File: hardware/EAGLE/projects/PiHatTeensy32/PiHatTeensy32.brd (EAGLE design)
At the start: 100 x 80 mm, 16 parts, among them T4 BM08B-SRSS-TB, U1 TSR_1-2450, X1 RASPI_BOARD_B+_H

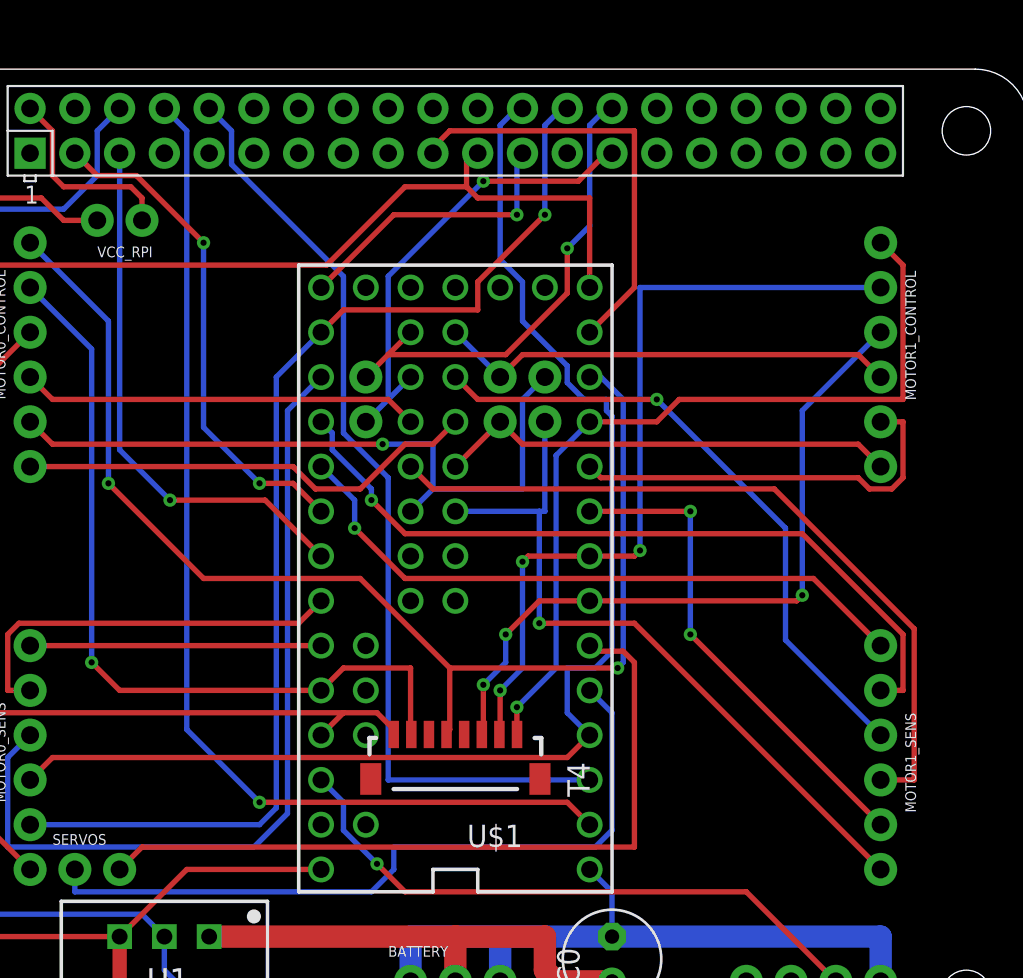
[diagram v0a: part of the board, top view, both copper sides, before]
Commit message: cancelled UART, made some cosmetic changes, ready for production
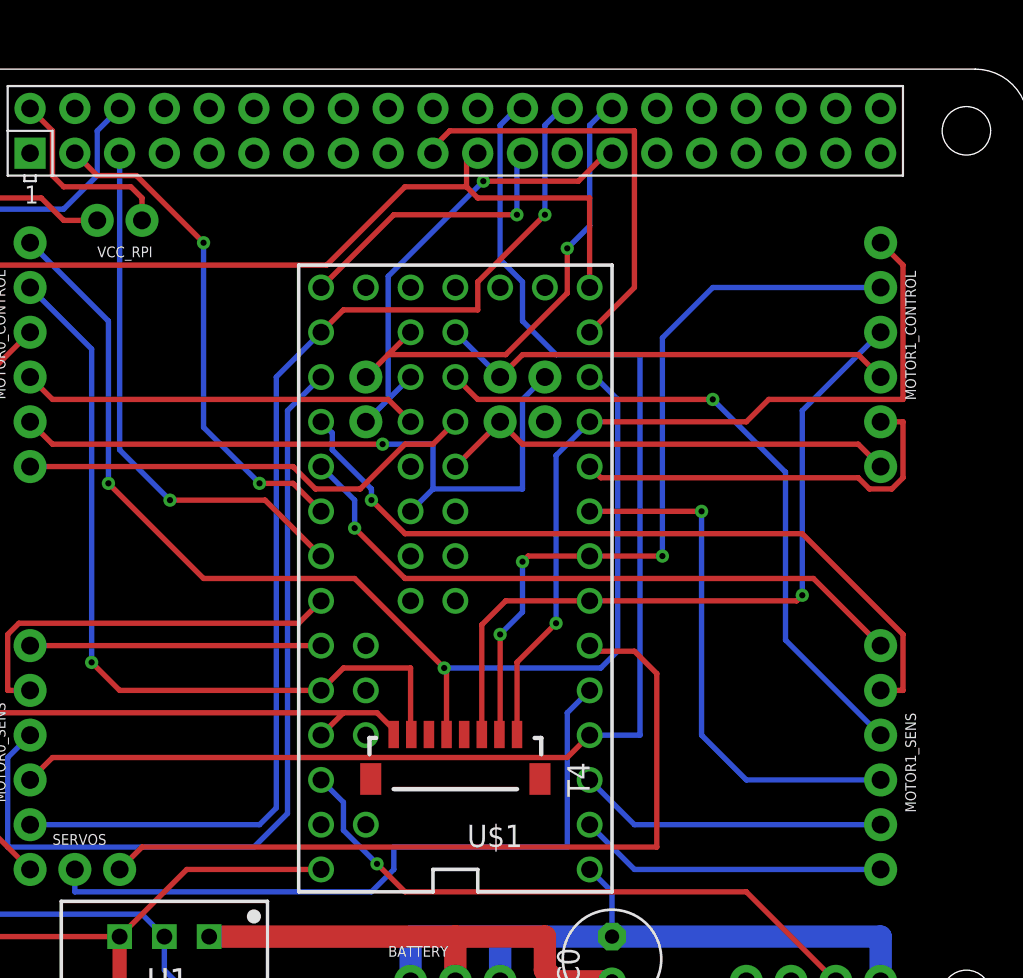
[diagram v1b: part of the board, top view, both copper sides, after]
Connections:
- net HALL_U1: now also U$1.0; no longer T4-32-33.1, U$1.24
- net HALL_V1: now also U$1.1; no longer U$1.7
- net HALL_W1: now also U$1.7; no longer U$1.32
- net PI_RX: no longer U$1.1
- net PI_TX: no longer U$1.0
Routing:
- net PI_TX: track 60.9 -> 0.00 mm, vias 1 -> 0
- net PI_RX: track 53.7 -> 0.00 mm
- net HALL_U1: track 41.7 -> 17.6 mm, vias 1 -> 0
- net HALL_W1: track 42.9 -> 30.3 mm, vias 0 -> 1
- net HALL_V1: track 28.0 -> 17.6 mm, vias 2 -> 0
- net HALL_W0_&_SPI_CS0: track 75.0 -> 78.0 mm
- net SERVO_1: track 43.2 -> 45.4 mm
- net SERVO_0: track 42.4 -> 40.4 mm
- net IS_U1: track 36.3 -> 38.1 mm
- net IN_V1: track 45.8 -> 44.4 mm
- net IN_U1: track 40.7 -> 41.9 mm, vias 3 -> 1
- net IN_W0: track 70.4 -> 69.4 mm

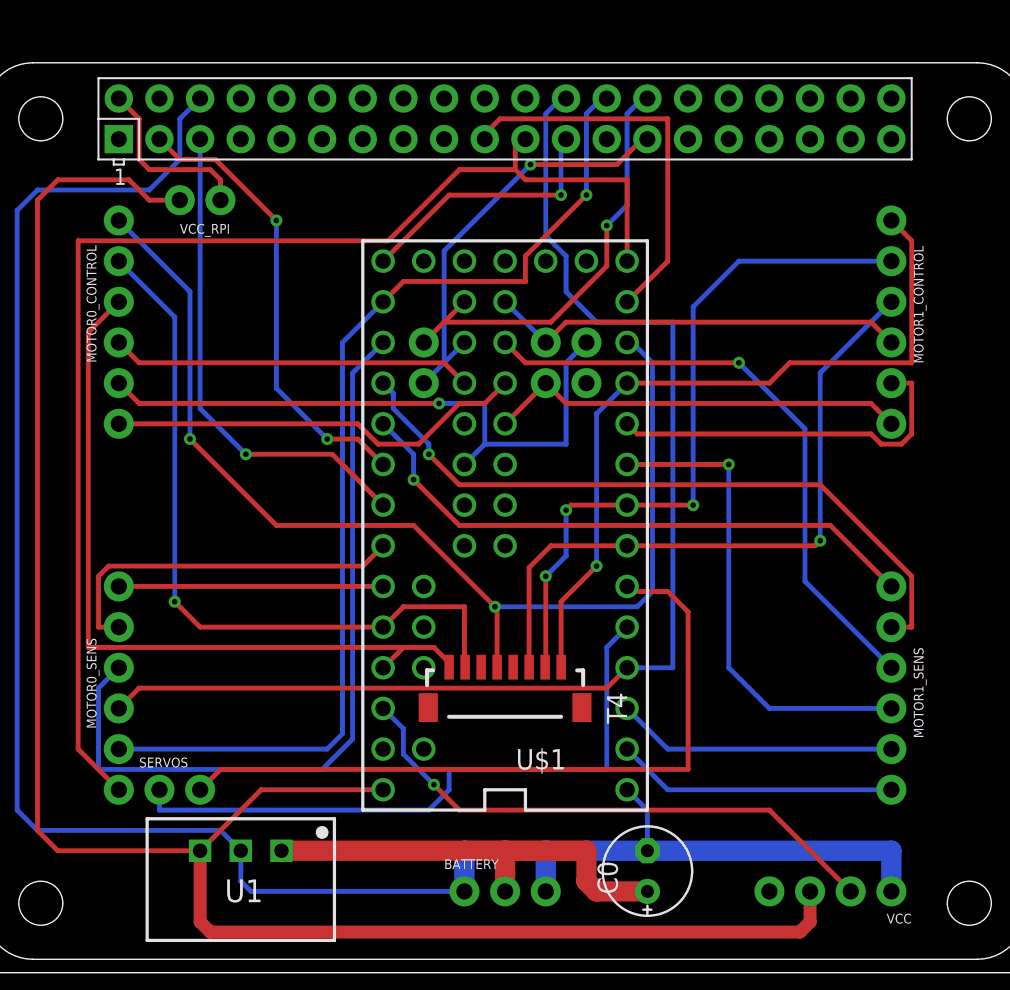
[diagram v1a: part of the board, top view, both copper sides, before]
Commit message: uart tx tx added back again, more coesmetic changes
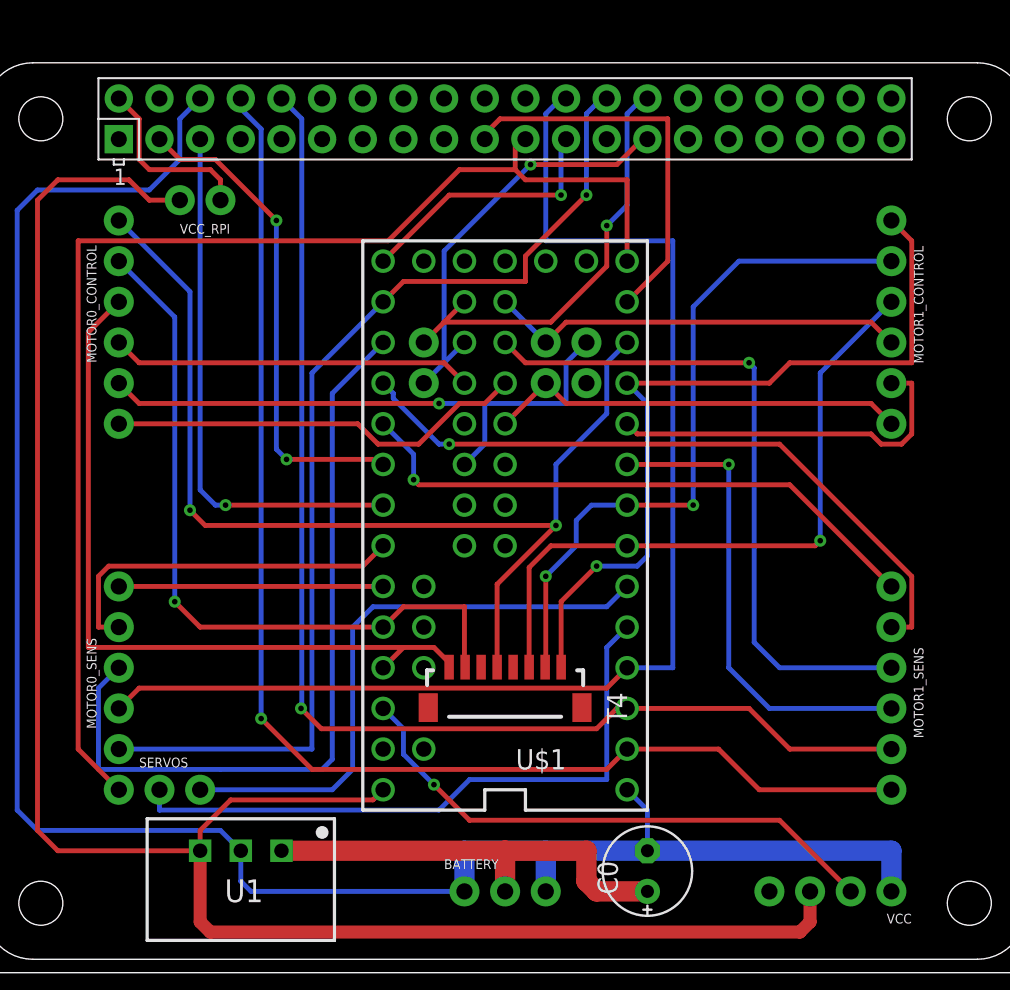
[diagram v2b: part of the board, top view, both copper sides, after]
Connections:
- removed net HALL_U1: MOTOR1_SENS.1, U$1.0
- removed net HALL_V1: MOTOR1_SENS.2, U$1.1
- removed net PI_RX: X1.10
- removed net PI_TX: X1.8
- new net HALL_U1_&_PI_TX: MOTOR1_SENS.1, U$1.0, X1.8
- new net HALL_V1_&PI_RX: MOTOR1_SENS.2, U$1.1, X1.10
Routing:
- net HALL_U1_&_PI_TX: track 0.00 -> 81.5 mm, vias 0 -> 1
- net HALL_V1_&PI_RX: track 0.00 -> 77.7 mm, vias 0 -> 1
- net HALL_V1: track 17.6 -> 0.00 mm
- net HALL_U1: track 17.6 -> 0.00 mm
- net SERVO_1: track 45.4 -> 37.2 mm
- net IS_U1: track 38.1 -> 42.6 mm
- net I2C0_SCL: track 30.8 -> 33.7 mm
- net INH_V0: track 39.7 -> 37.1 mm
- net IN_W1: track 47.2 -> 49.7 mm
- net IN_W0: track 69.4 -> 66.8 mm
- net I2C0_SDA: track 28.5 -> 30.8 mm
- net HALL_W0_&_SPI_CS0: track 78.0 -> 79.9 mm
- net 5.0V: track 118.0 -> 118.7 mm
- net IN_V1: track 44.4 -> 43.6 mm, vias 3 -> 2
- net IS_V1: track 43.4 -> 42.6 mm
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
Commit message: Label added to PiHatTeensy32
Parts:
- renumbered U$1 to TEENSY, U1 to DC-DC
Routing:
- net IS_W1: track 36.9 -> 39.1 mm
- net IS_V1: track 42.6 -> 44.8 mm
- net INH_V1: track 23.0 -> 23.9 mm
- net GND: track 123.1 -> 122.6 mm
- net IN_V0: track 46.3 -> 45.8 mm
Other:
- board text added: "00 HALL_U1"
- board text added: "01 HALL_V1"
- board text added: "05 IN_U1"
- board text added: "06 IN_V1"
- board text added: "07 HALL_W1"
- board text added: "08 INH_V1"
- board text added: "09 IN_W1"
- board text added: "16 IS_V1"
- board text added: "17 IS_W1"
- board text added: "25 INH_U1"
- board text added: "27 IS_U1"
- board text added: "28 INH_W1"
- board text added: "3.3V"
- board text added: "5.0V"
- board text added: "6-24V"
- board text added: "GND"
- board text added: "HALL_U0 12"
- board text added: "HALL_V0 14"
- board text added: "HALL_W0 02"
- board text added: "INH_U0 26"
- board text added: "INH_V0 33"
- board text added: "INH_W0 31"
- board text added: "IN_U0 23"
- board text added: "IN_V0 22"
- board text added: "IN_W0 10"
- board text added: "IS_U0 15"
- board text added: "IS_V0 20"
- board text added: "IS_W0 21"
- board text added: "RPiTeensy v.2020-03"
- board text added: "Servo0 03"
- board text added: "Servo1 04"
- board text added: "VCC"
